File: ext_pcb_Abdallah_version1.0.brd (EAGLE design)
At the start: 100 x 100 mm, 38 parts, among them CN10 MCV_05/4-G-2,5V, CN11 MCV_05/4-G-2,5V, CN12 MCV_05/4-G-2,5V, CN13 MCV_05/4-G-2,5V, CN15 MCV_05/2-G-2,5V, CN16 MCV_05/2-G-2,5V, CN17 MCV_05/2-G-2,5V, CN2 53047-08, CN3 53047-06, CN4 MCV_05/4-G-2,5V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

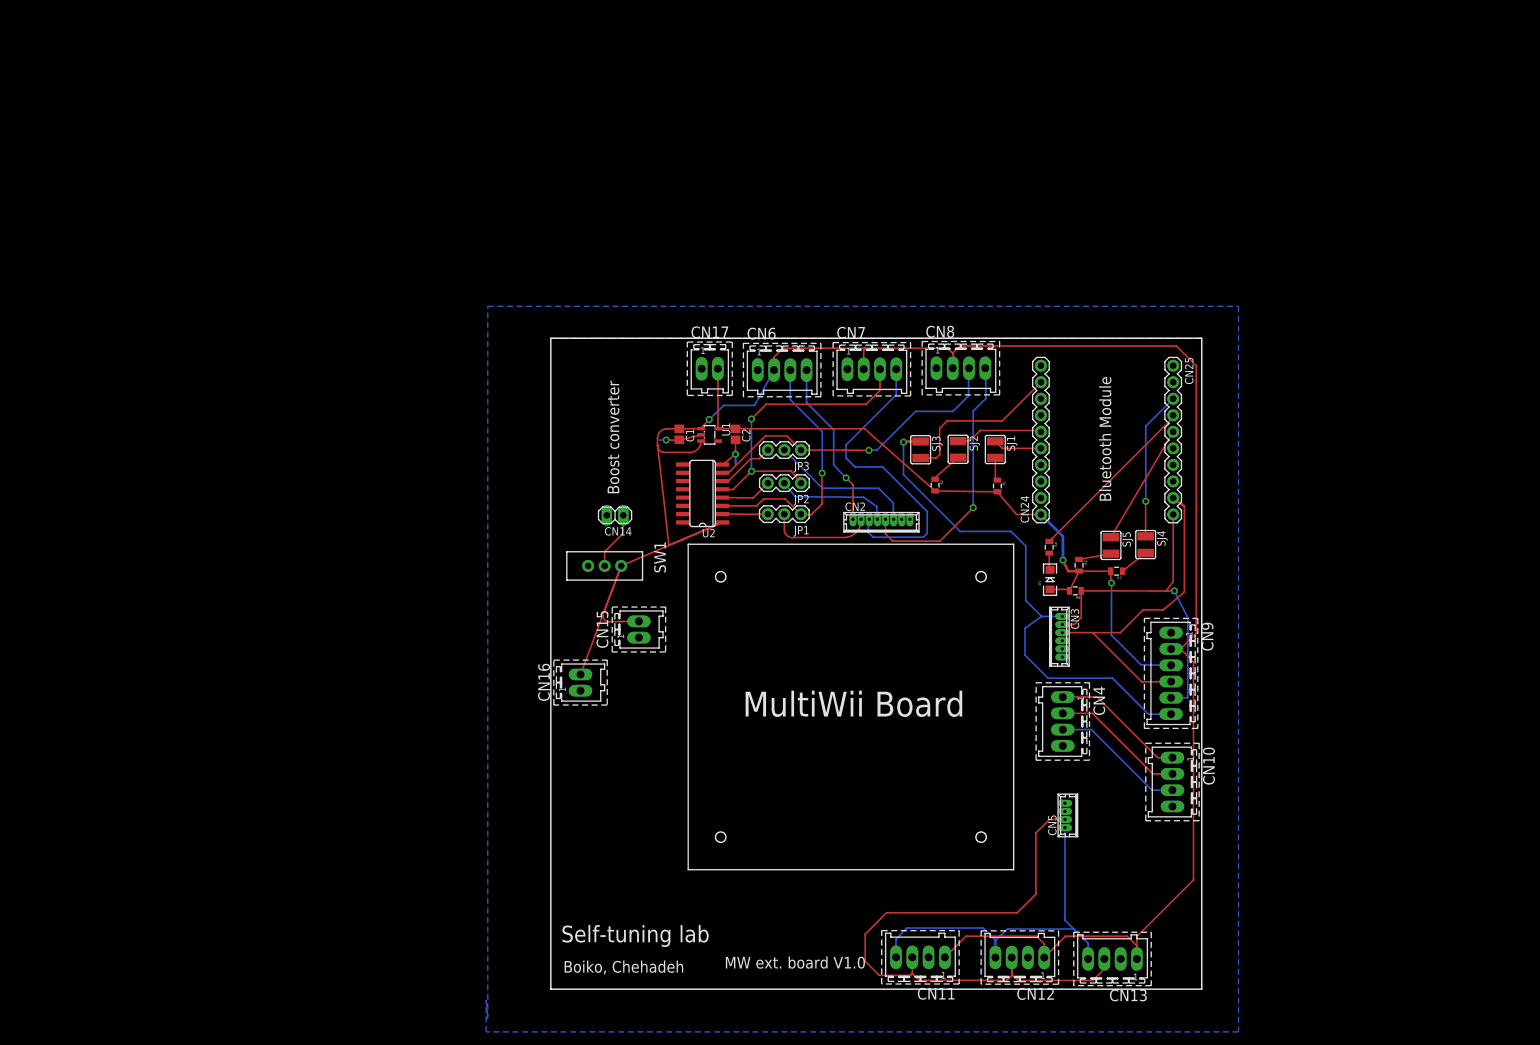
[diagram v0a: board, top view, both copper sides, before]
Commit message: Finish PCB traces
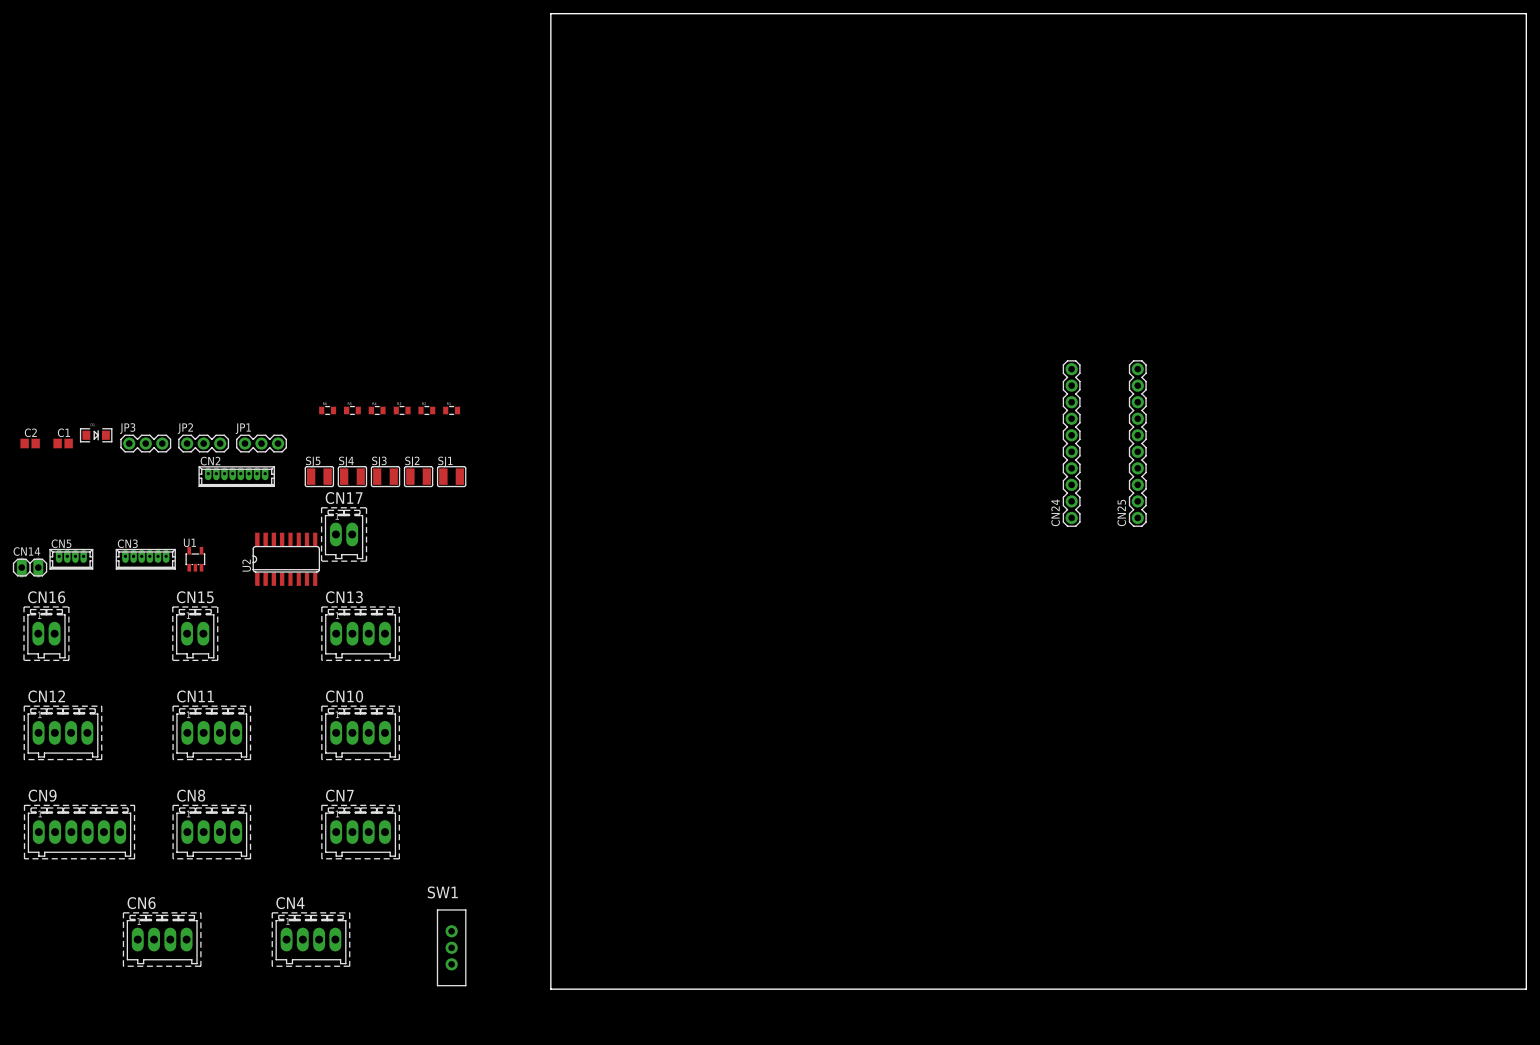
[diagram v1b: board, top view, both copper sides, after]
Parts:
- moved CN9 170.9 mm to (-73.7, 24.1), turned to 0 degrees
- moved CN5 158.1 mm to (-73.7, 66.0), turned to 0 degrees
- moved CN12 153.4 mm to (-76.2, 39.4), turned to 0 degrees
- moved D1 148.2 mm to (-69.8, 85.1), turned to 0 degrees
- moved CN3 140.9 mm to (-62.2, 66.0), turned to 0 degrees
- moved CN8 135.4 mm to (-53.3, 24.1)
- moved CN6 129.3 mm to (-61.0, 7.62)
- moved CN13 128.2 mm to (-30.5, 54.6), turned to 0 degrees
- moved CN10 126.1 mm to (-30.5, 39.4), turned to 0 degrees
- moved SJ4 122.3 mm to (-30.5, 78.7), turned to 0 degrees
- moved SJ5 122.1 mm to (-35.6, 78.7), turned to 0 degrees
- moved CN4 121.8 mm to (-38.1, 7.62), turned to 0 degrees
- moved R6 118.2 mm to (-34.3, 88.9), turned to 0 degrees
- moved CN11 116.6 mm to (-53.3, 39.4), turned to 0 degrees
- moved R5 114.1 mm to (-30.5, 88.9), turned to 0 degrees
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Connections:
- removed net CN2_GND: CN2.1
- removed net CN3_GND: CN3.1, CN3.2
- removed net CN4_GND: CN4.4
- removed net CN5_GND: CN5.1
- net GND: now also CN2.1, CN3.1, CN3.2, CN4.4, CN5.1
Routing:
- net VCC: track 316.1 -> 0.00 mm, vias 1 -> 0
- net V3_3: track 108.3 -> 0.00 mm, vias 2 -> 0
- net MW_SDA: track 96.6 -> 0.00 mm
- net MW_DTR: track 79.5 -> 0.00 mm, vias 1 -> 0
- net MW_SCL: track 59.2 -> 0.00 mm
- net MW_TX0: track 53.3 -> 0.00 mm, vias 1 -> 0
- net MW_RX0: track 51.7 -> 0.00 mm
- net MW_RX3IN: track 48.8 -> 0.00 mm, vias 1 -> 0
- net MW_TX2: track 47.7 -> 0.00 mm
- net MW_RX2IN: track 47.2 -> 0.00 mm, vias 2 -> 0
- net MW_TX3: track 40.6 -> 0.00 mm, vias 1 -> 0
- net MW_RX1IN: track 39.9 -> 0.00 mm, vias 1 -> 0
- net N$11: track 27.3 -> 0.00 mm
- net MW_TX1: track 25.9 -> 0.00 mm, vias 1 -> 0
- net N$1: track 25.7 -> 0.00 mm
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- removed copper zone on layer 16, net GND
- removed copper zone on layer 16, net N$9
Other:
- board size 100 x 100 mm -> 149.9 x 149.9 mm
- board text removed: "Bluetooth Module"
- board text removed: "Boiko, Chehadeh"
- board text removed: "Boost converter"
- board text removed: "MW ext. board V1.0"
- board text removed: "MultiWii Board"
- board text removed: "Self-tuning lab"
